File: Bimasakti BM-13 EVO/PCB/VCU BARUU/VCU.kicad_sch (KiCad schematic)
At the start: 20 parts, among them Q1 IRLZ44N, Q2 IRLZ44N, Q3 IRLZ44N, U1 Teensy4.1, U2 SN65HVD230, U3 SN65HVD230, U4 ADS1115IDGS, U5 SN65HVD230

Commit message: cicil assembly
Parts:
- removed Q1, Q2, Q3: IRLZ44N, Package_TO_SOT_THT:TO-220-3_Vertical, symbol Transistor_FET:IRLZ44N
- added C2: 0.1uF, Capacitor_SMD:C_0603_1608Metric, symbol Device:C
- added J1: 6437288-3, 0_VCU_CONNECTOR_TE_6437288-3:VCU_CONNECTOR_TE_6437288-3, symbol 0_VCU_connector_6437288-3:6437288-3
- added R12, R13, R14, R15: 5k, Resistor_SMD:R_0805_2012Metric, symbol Device:R
- added R16, R17: 10K, Resistor_SMD:R_0805_2012Metric, symbol Device:R
- added U10, U6, U7, U8, U9: ~, Package_TO_SOT_SMD:TO-252-2, symbol 0_MOSFETs:DMTH6016LK3
- added U11: ADS1115IDGS, Package_SO:TSSOP-10_3x3mm_P0.5mm, symbol Analog_ADC:ADS1115IDGS
- R10, R11, R9: value 1K -> 5k
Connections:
- net 3V3: now also U1.46 (3V3), C2.2, R14.1, R15.1, R16.1, R17.1, U11.8 (VDD)
- net ANA_GND: now also C2.1, U11.1 (ADDR), U11.3 (GND)
- net BAT_FAN: now also J1.11, U8.1 (D)
- net BRAKE_LIGHT: now also U7.1 (D)
- net D1: now also U8.2 (G)
- net D2: now also U6.2 (G)
- net D3: now also U7.2 (G)
- net GND: now also U1.1 (GND), J1.14, R12.2, R13.2, U10.3 (S), U6.3 (S), U7.3 (S), U8.3 (S), U9.3 (S)
- net SCL: now also R17.2, U11.10 (SCL)
- net SDA: now also R16.2, U11.9 (SDA)
- net SWITCH_AIR: now also U6.1 (D)
- net SUSP1: now reaches U4.4 (AIN0)
- net SUSP1: now also J1.7
- net SUSP2: now reaches U4.5 (AIN1)
- net SUSP2: now also J1.8
- net SUSP3: now reaches U4.6 (AIN2)
- net SUSP3: now also J1.9
- net SUSP4: now reaches U4.7 (AIN3)
- net SUSP4: now also J1.10
- new net 12V: J1.13
- new net AIR: J1.4
- new net AIR SWITCH: R15.2, U9.2 (G)
- new net AIR_RELAYGND: R12.1, U9.1 (D)
- new net AMB_TEMP: J1.12
- new net APPS1: J1.41
- new net APPS2: J1.42
- new net BMS_CAN: J1.1
- new net BRK_LIGHT: J1.2
- new net BRK_PRESS: J1.3, U11.4 (AIN0)
- new net ENG SWITCH: R14.2, U10.2 (G)
- new net ENG_RELAYGND: R13.1, U10.1 (D)
- new net ENG_RLY: J1.6
- new net ESC_CAN1: J1.35
- new net ESC_CAN2: J1.36
- new net GPOS: J1.44
- new net STEER: J1.43
- new net SWITCH_HY: J1.5
- new net WS1: J1.37
- new net WS2: J1.38
- new net WS3: J1.39
- new net WS4: J1.40
- no-connect marks 68 -> 66

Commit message: Aku Telemetry
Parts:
- removed J1: 6437288-3, 0_VCU_CONNECTOR_TE_6437288-3:VCU_CONNECTOR_TE_6437288-3, symbol 0_VCU_connector_6437288-3:6437288-3
- added C3, C4, C5, C6, C7: 0.1uF, Capacitor_SMD:C_0603_1608Metric, symbol Device:C
- added U12: DEV-16771, Teensy:Teensy41, symbol DEV-16771:DEV-16771
- R1, R2: value R -> 120
- R16, R17, R5, R6: value 10K -> 4.7K
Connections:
- net BRK_PRESS: now also C7.2
- net GND: now also C3.2, C4.2, C5.1, C6.1, C7.1
- net SUSP1: now also C3.1
- net SUSP2: now also C4.1
- net SUSP3: now also C5.2
- net SUSP4: now also C6.2
- new net: U12.3.3V_1 (3.3V), U12.3.3V_2 (3.3V), U12.3.3V_3 (3.3V)
- new net: U12.GND1 (GND), U12.GND2 (GND), U12.GND3 (GND), U12.GND4 (GND), U12.GND5 (GND)
- new net: U12.USB_GND1 (USB_GND), U12.USB_GND2 (USB_GND)
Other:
- moved on the sheet: C1, C2, R10, R11, R12, R13, R14, R15, R16, R17, R2, R4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

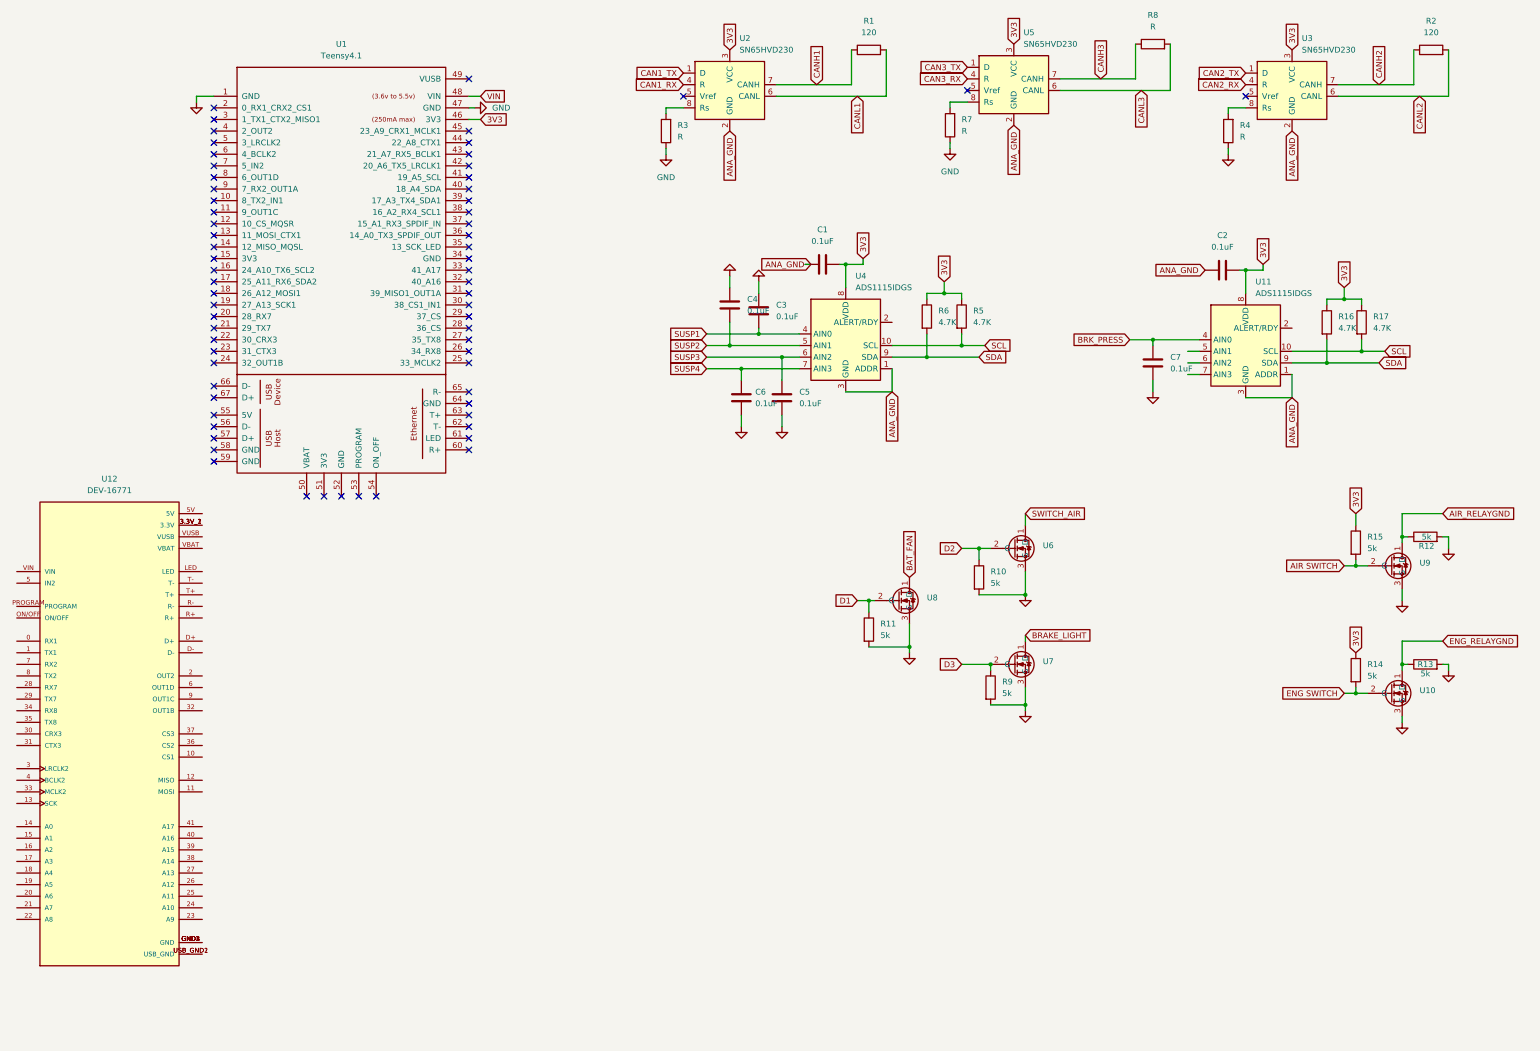
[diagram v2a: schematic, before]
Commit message: buat placeholder baru dan ganti konektor
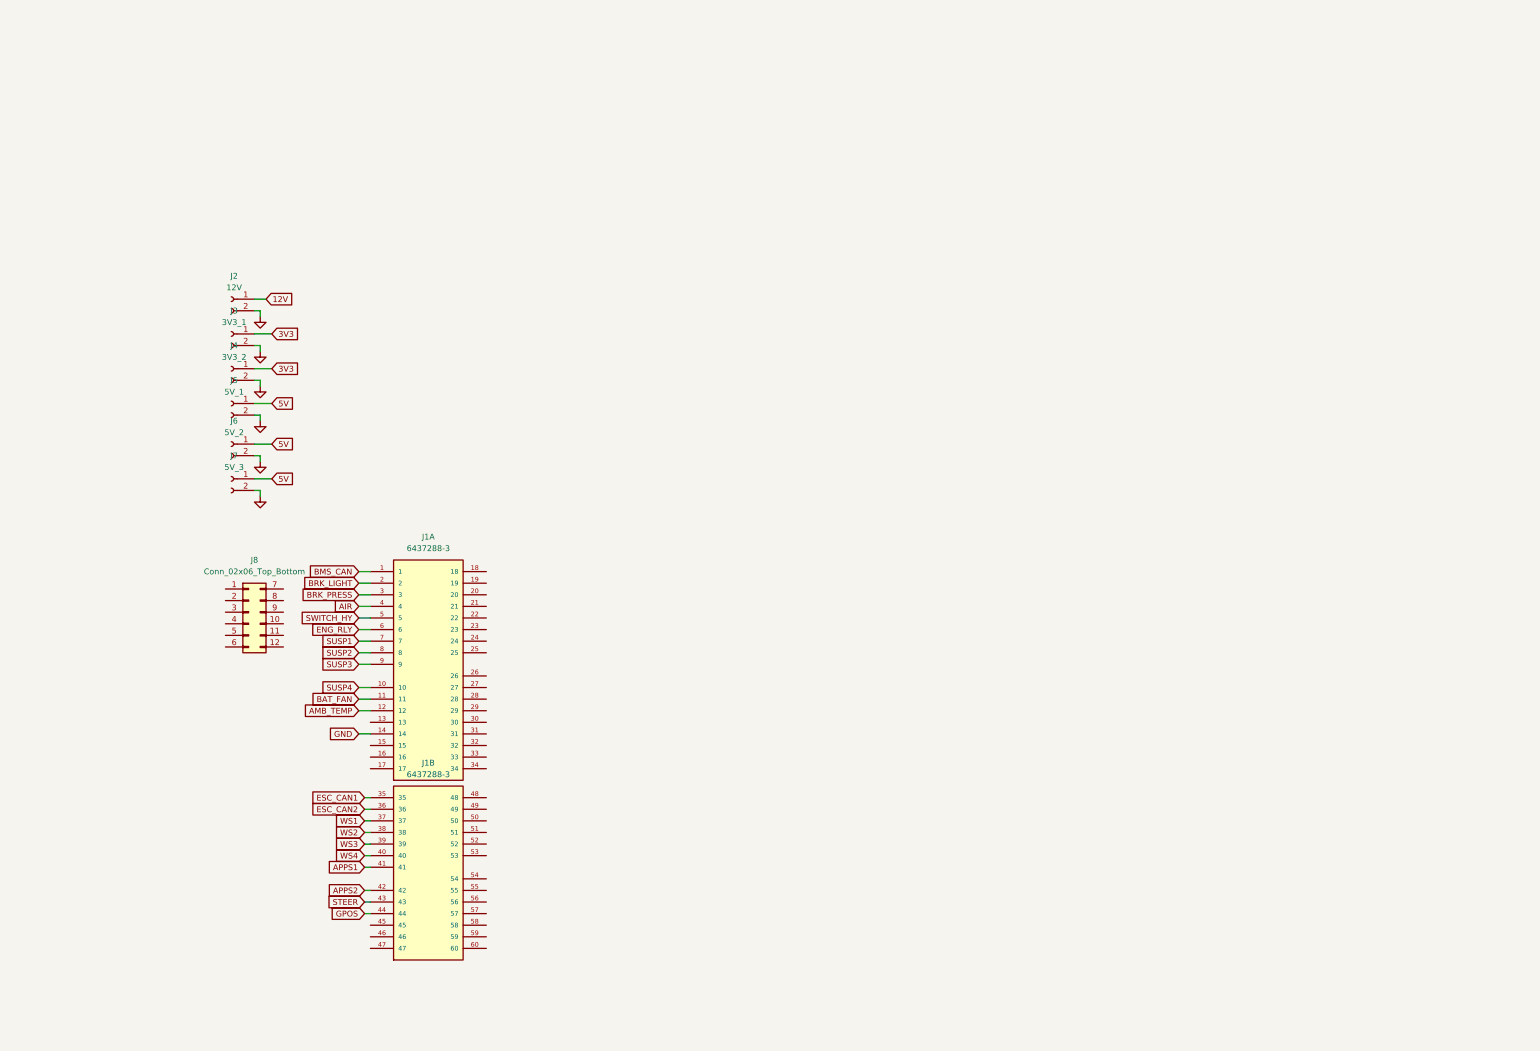
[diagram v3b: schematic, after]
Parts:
- removed C1, C2, C3, C4, C5, C6, C7: 0.1uF, Capacitor_SMD:C_0603_1608Metric, symbol Device:C
- removed R1, R2: 120, Resistor_SMD:R_0805_2012Metric, symbol Device:R
- removed R10, R11, R12, R13, R14, R15, R9: 5k, Resistor_SMD:R_0805_2012Metric, symbol Device:R
- removed R16, R17, R5, R6: 4.7K, Resistor_SMD:R_0805_2012Metric, symbol Device:R
- removed R3, R4, R7, R8: R, Resistor_SMD:R_0805_2012Metric, symbol Device:R
- removed U1: Teensy4.1, Teensy:Teensy41, symbol teensy:Teensy4.1
- removed U10, U6, U7, U8, U9: ~, Package_TO_SOT_SMD:TO-252-2, symbol 0_MOSFETs:DMTH6016LK3
- removed U11, U4: ADS1115IDGS, Package_SO:TSSOP-10_3x3mm_P0.5mm, symbol Analog_ADC:ADS1115IDGS
- removed U12: DEV-16771, Teensy:Teensy41, symbol DEV-16771:DEV-16771
- removed U2, U3, U5: SN65HVD230, Package_SO:SOIC-8_3.9x4.9mm_P1.27mm, symbol Interface_CAN_LIN:SN65HVD230
- added J1: 6437288-3, 0_VCU_CONNECTOR_TE_6437288-3:VCU_CONNECTOR_TE_6437288-3, symbol 0_VCU_connector_6437288-3:6437288-3
- added J2: 12V, Connector_JST:JST_XH_B2B-XH-A_1x02_P2.50mm_Vertical, symbol Connector:Conn_01x02_Socket
- added J3: 3V3_1, Connector_JST:JST_XH_B2B-XH-A_1x02_P2.50mm_Vertical, symbol Connector:Conn_01x02_Socket
- added J4: 3V3_2, Connector_JST:JST_XH_B2B-XH-A_1x02_P2.50mm_Vertical, symbol Connector:Conn_01x02_Socket
- added J5: 5V_1, Connector_JST:JST_XH_B2B-XH-A_1x02_P2.50mm_Vertical, symbol Connector:Conn_01x02_Socket
- added J6: 5V_2, Connector_JST:JST_XH_B2B-XH-A_1x02_P2.50mm_Vertical, symbol Connector:Conn_01x02_Socket
- added J7: 5V_3, Connector_JST:JST_XH_B2B-XH-A_1x02_P2.50mm_Vertical, symbol Connector:Conn_01x02_Socket
- added J8: Conn_02x06_Top_Bottom, Connector_Molex:Molex_Nano-Fit_105310-xx12_2x06_P2.50mm_Vertical, symbol Connector_Generic:Conn_02x06_Top_Bottom
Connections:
- net 3V3: now also J3.1 (Pin_1), J4.1 (Pin_1)
- net BAT_FAN: now also J1.11
- net BRK_PRESS: now also J1.3
- net GND: now also J1.14, J2.2 (Pin_2), J3.2 (Pin_2), J4.2 (Pin_2), J5.2 (Pin_2), J6.2 (Pin_2), J7.2 (Pin_2)
- net SUSP1: now also J1.7
- net SUSP2: now also J1.8
- net SUSP3: now also J1.9
- net SUSP4: now also J1.10
- new net 12V: J2.1 (Pin_1)
- new net 5V: J5.1 (Pin_1), J6.1 (Pin_1), J7.1 (Pin_1)
- new net AIR: J1.4
- new net AMB_TEMP: J1.12
- new net APPS1: J1.41
- new net APPS2: J1.42
- new net BMS_CAN: J1.1
- new net BRK_LIGHT: J1.2
- new net ENG_RLY: J1.6
- new net ESC_CAN1: J1.35
- new net ESC_CAN2: J1.36
- new net GPOS: J1.44
- new net STEER: J1.43
- new net SWITCH_HY: J1.5
- new net WS1: J1.37
- new net WS2: J1.38
- new net WS3: J1.39
- new net WS4: J1.40
- no-connect marks 66 -> 0

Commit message: assembly kurang pneumatic, kurang wiring dudukan motherboard
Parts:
- added BSPD1: ~, 0_FootPrintBPSD:FootPrintBPSD, symbol 0_BSPDFootprint:FootprintBSPD
- added J10: Conn_01x02_Socket, Connector_Molex:Molex_Nano-Fit_105309-xx02_1x02_P2.50mm_Vertical, symbol Connector:Conn_01x02_Socket
- added J9: SIGNAL 2, Connector_Molex:Molex_Nano-Fit_105310-xx12_2x06_P2.50mm_Vertical, symbol Connector_Generic:Conn_02x06_Top_Bottom
- added U1: ~, 0_FootprintTelemetry:0_FootprintTelemetry, symbol 0_FootprintTelemetry:FootprintTelemetry
- added U2: ~, 0_FootprintVCU:FootprintVCU, symbol 0_FootprintVCU:FootprintVCU
- J8: value Conn_02x06_Top_Bottom -> SIGNAL 1
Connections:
- net ESC_CAN1 is gone; now on net ESC1_HI: J1.35
- net ESC_CAN2 is gone; now on net ESC1_LO: J1.36
- net 12V: now also J10.1 (Pin_1), U2.1 (+12V)
- net 5V: now also BSPD1.7 (+5V), U1.6 (+5V), U2.29 (+5V)
- net AIR: now also J1.57, U2.7 (AIR); no longer J1.4
- net BRK_PRESS: now also BSPD1.6 (BrakePress), U2.45 (Brake_pressure)
- net ENG_RLY: now also U2.3 (Engine); no longer J1.6
- net GND: now also J8.7 (Pin_7), BSPD1.10 (GND), BSPD1.11 (GND), BSPD1.12 (GND), BSPD1.13 (GND), BSPD1.14 (GND), J10.2 (Pin_2), U1.1 (GND), U1.11 (GND), U1.12 (GND), U1.13 (GND), U1.14 (GND), U1.15 (GND), U1.16 (GND), U1.2 (GND), U1.3 (GND), U1.4 (GND), U1.5 (GND), U2.13 (GND), U2.15 (GND), U2.17 (GND), U2.18 (GND), U2.2 (GND), U2.20 (GND), U2.22 (GND), U2.24 (GND), U2.26 (GND), U2.30 (GND), U2.31 (GND), U2.34 (GND), U2.37 (GND), U2.40 (GND), U2.41 (GND), U2.50 (GND), U2.53 (GND), U2.56 (GND)
- net GPOS: no longer J1.44
- net SUSP1: now also U2.49 (SUS1)
- net SUSP2: now also U2.48 (SUS2)
- net SUSP3: now also U2.47 (SUS3)
- net SUSP4: now also U2.46 (SUS4)
- net SWITCH_HY: now also J1.56, U2.6 (Hybrid); no longer J1.5
- net WS1: now also J1.39; no longer J1.37
- net WS2: no longer J1.38
- net WS3: no longer J1.39
- net WS4: no longer J1.40
- net SCK: now reaches J8.1 (Pin_1)
- net STEER_IN: now reaches J8.10 (Pin_10)
- net APPS_IN2: now reaches J8.11 (Pin_11)
- net APPS_IN1: now reaches J8.12 (Pin_12)
- net MISO: now reaches J8.2 (Pin_2)
- net MOSI: now reaches J8.3 (Pin_3)
- net SS: now reaches J8.4 (Pin_4)
- net STM_TX: now reaches J8.5 (Pin_5)
- net STM_TX: now also U2.14 (TX_TV)
- net STM_RX: now reaches J8.6 (Pin_6)
- net STM_RX: now also U2.16 (RX_TV)
- net ESC1_LO: now reaches J8.8 (Pin_8)
- net ESC1_HI: now reaches J8.9 (Pin_9)
- net COM_BSPD: now reaches J1.18
- net NC_BSPD: now reaches J1.19
- net ECU_HI: now reaches J1.20
- net ECU_HI: now also U2.32 (CANH_2)
- net ECU_LO: now reaches J1.21
- net ECU_LO: now also U2.33 (CANL_2)
- net BMS_HI: now reaches J1.22
- net BMS_HI: now also U2.35 (CANH_1)
- net BMS_LO: now reaches J1.23
- net BMS_LO: now also U2.36 (CANL_1)
- net DISP_HI: now reaches J1.24
- net DISP_HI: now also U2.38 (CANH_3)
- net DISP_LO: now reaches J1.25
- net DISP_LO: now also U2.39 (CANL_3)
- net SDC_IN: now reaches J1.32
- net SDC_IN: now also U2.9 (SDC_IN)
- net SDC_OUT: now reaches J1.33
- net SDC_OUT: now also U2.10 (SDC_OUT)
- net FAN_BATT: now reaches J1.48
- net FAN_BATT: now also U2.12 (FAN_BATT)
- net SAFETY: now reaches J1.52
- net SAFETY: now also J1.58, U2.5 (Safety), U2.8 (Safety)
- net PDM: now reaches J1.59
- net PDM: now also U2.4 (PDM)
- net ENGINE: now reaches J1.60
- net APPS1: no longer names the net of J1.41
- net APPS2: no longer names the net of J1.42
- net BRK_LIGHT renamed BRAKE_LIGHT
- net BRAKE_LIGHT: now also U2.11 (Brake_Light)
- net STEER: no longer names the net of J1.43
- new net COM: BSPD1.4 (COM)
- new net CS_T: U1.10 (CS2), U2.19 (CS_T)
- new net ESC2_HI: J1.37, J9.11 (Pin_11)
- new net ESC2_LO: J1.38, J9.10 (Pin_10)
- new net MISO_T: U1.8 (MISO2), U2.23 (MISO_T)
- new net MOSI_T: U1.7 (MOSI2), U2.21 (MOSI_T)
- new net NC: BSPD1.3 (NC)
- new net SCK_T: U1.9 (SCK2), U2.25 (SCK_T)
- new net TPS: BSPD1.5 (ThrottlePos)
- new net WS_FL: J9.4 (Pin_4)
- new net WS_FR: J9.5 (Pin_5)
- new net WS_RL: J9.2 (Pin_2)
- new net WS_RR: J9.3 (Pin_3)
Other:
- moved on the sheet: J1A, J1B
